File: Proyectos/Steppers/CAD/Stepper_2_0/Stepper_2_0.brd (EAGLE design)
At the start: 151.1 x 97.8 mm, 91 parts

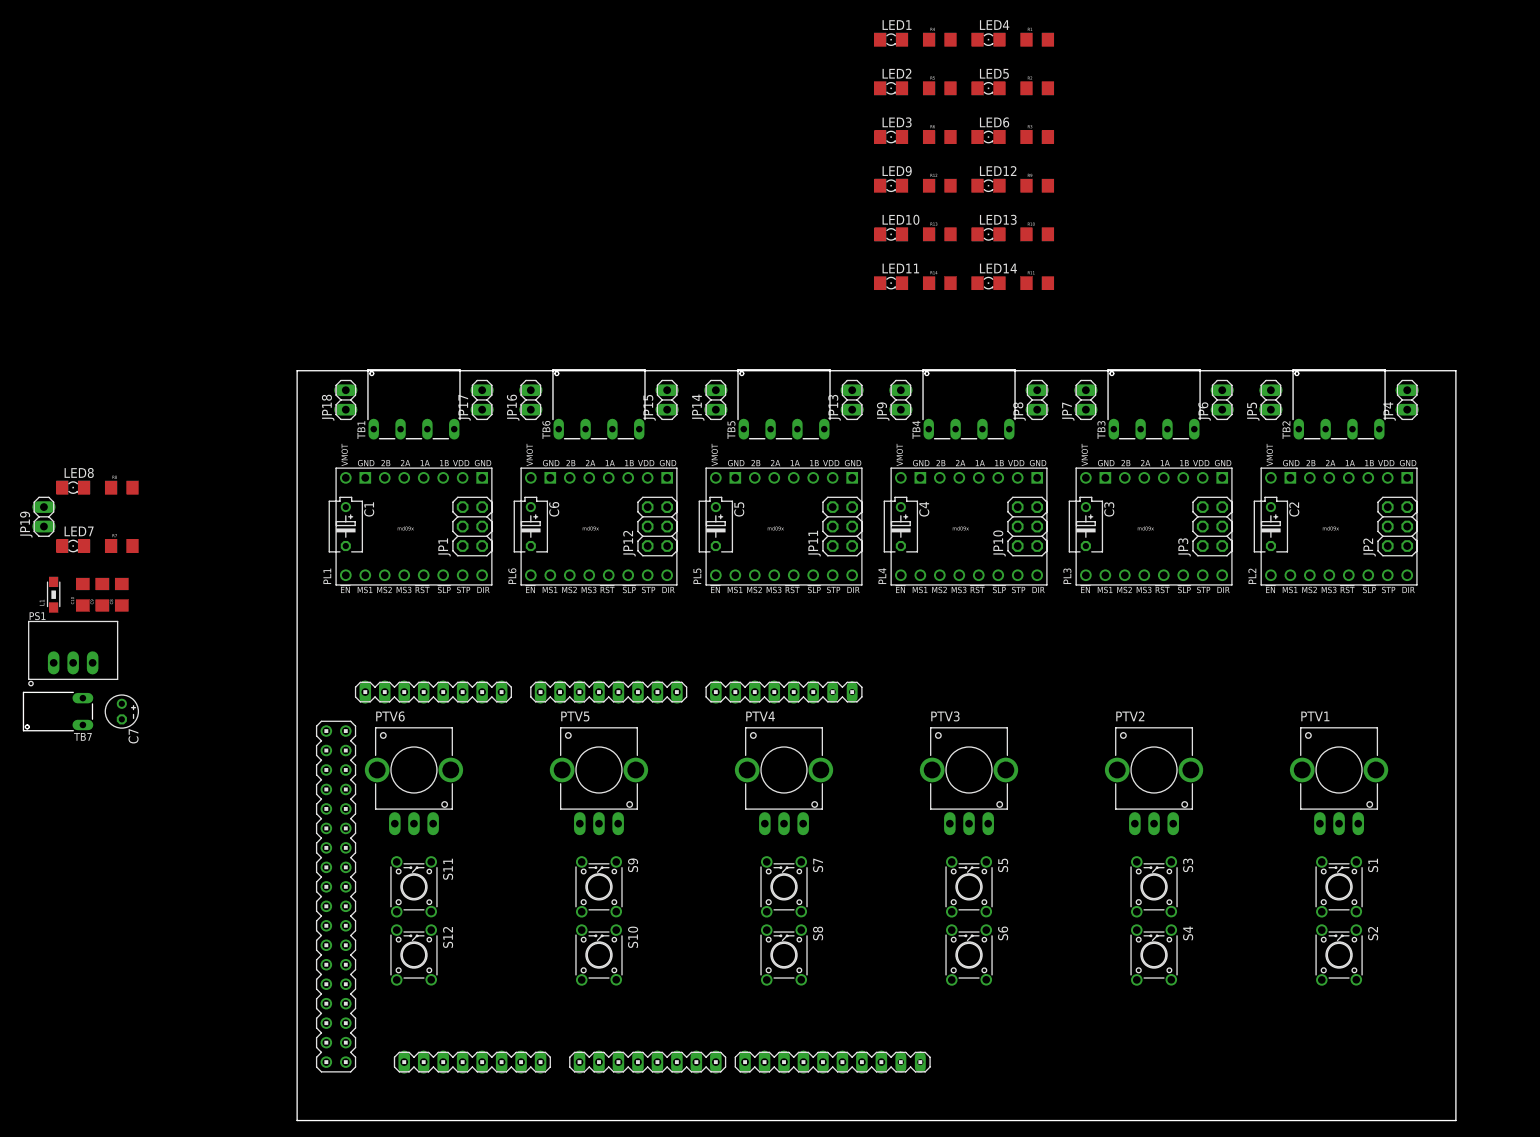
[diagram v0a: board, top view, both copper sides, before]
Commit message: Steppers:
Avance en PCB final, asignación de pines DUE.
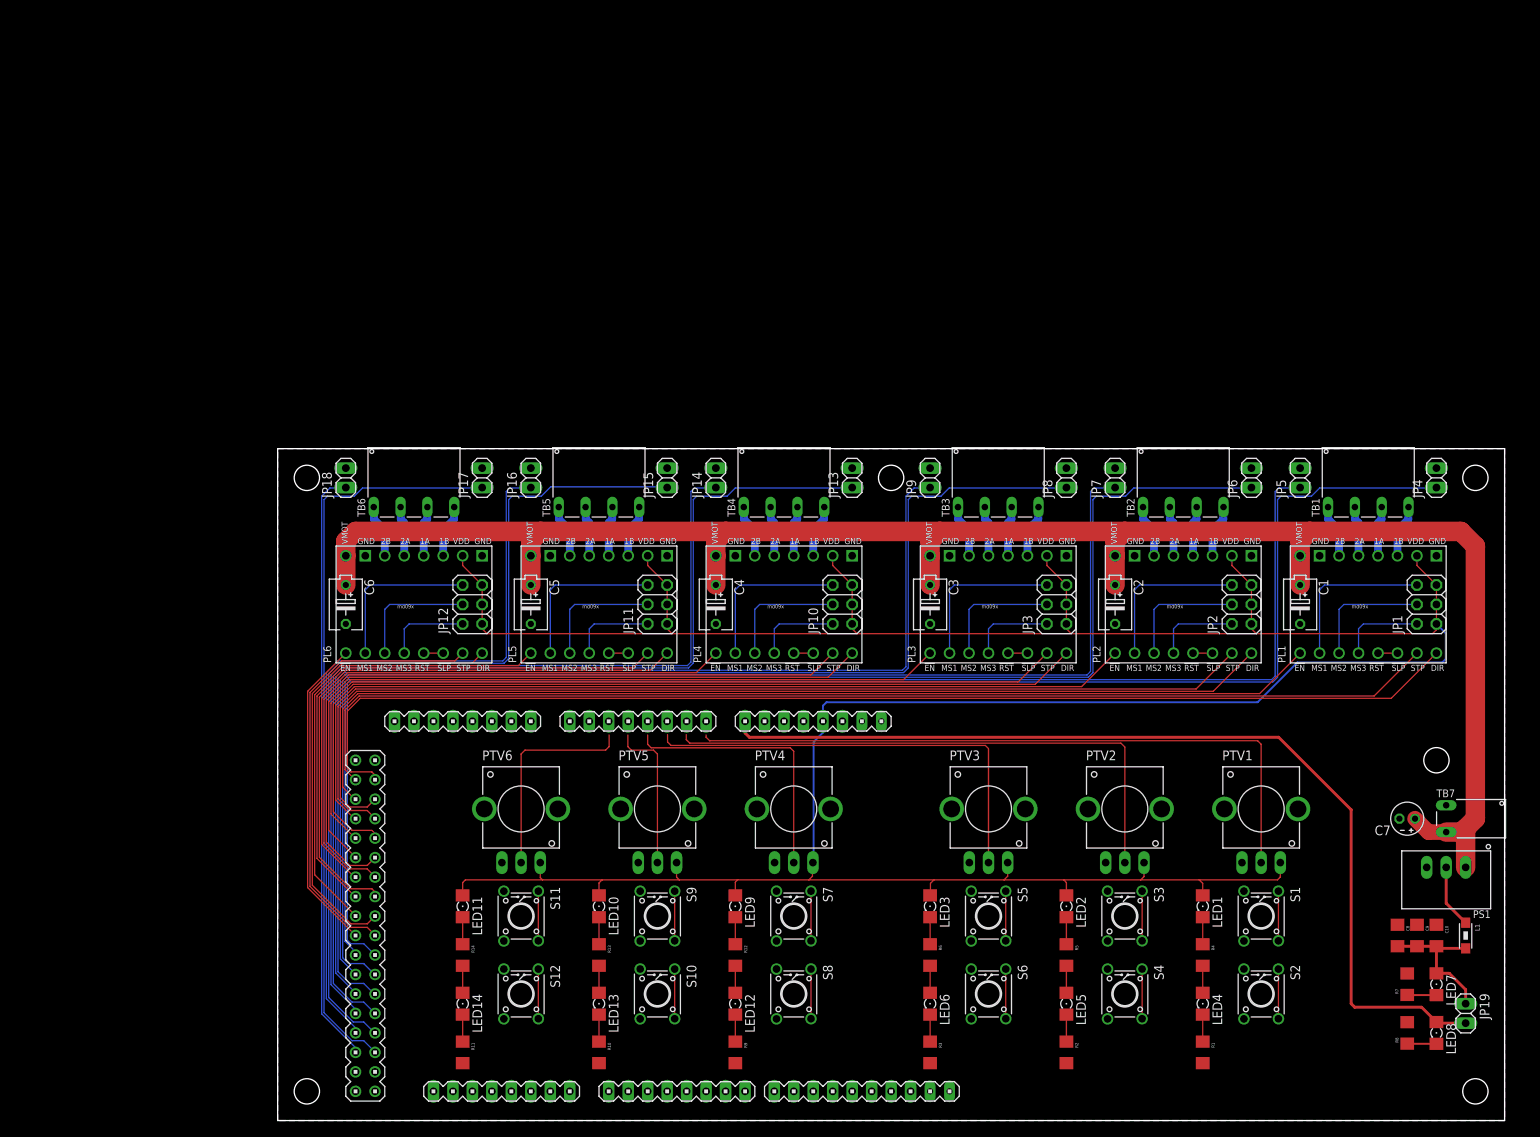
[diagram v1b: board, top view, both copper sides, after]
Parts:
- added H1, H2, H3, H4, H5, H6: STAND-OFF, SparkFun-Electromechanical:STAND-OFF
- moved JP19 196.4 mm to (152.4, 14.0), turned to 270 degrees
- moved LED8 191.5 mm to (148.6, 11.4), turned to 270 degrees
- moved L1 189.4 mm to (152.4, 24.1), turned to 270 degrees
- moved LED7 186.8 mm to (148.6, 17.8), turned to 270 degrees
- moved R8 182.1 mm to (144.8, 11.4), turned to 90 degrees
- moved C10 182.0 mm to (148.6, 24.1), turned to 270 degrees
- moved PS1 181.0 mm to (149.9, 33.0), turned to 180 degrees
- moved TB7 178.3 mm to (149.9, 39.4), turned to 270 degrees
- moved C9 177.1 mm to (146.1, 24.1), turned to 270 degrees
- moved R7 177.1 mm to (144.8, 17.8), turned to 90 degrees
- moved C8 172.2 mm to (143.5, 24.1), turned to 270 degrees
- moved C7 168.2 mm to (144.8, 39.4), turned to 180 degrees
- moved R1 133.8 mm to (118.1, 8.89), turned to 270 degrees
- moved LED4 128.8 mm to (118.1, 15.2), turned to 270 degrees
- moved R2 125.8 mm to (100.3, 8.89), turned to 270 degrees
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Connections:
- removed net N$12: LED1.A
- removed net N$14: LED2.A
- removed net N$25: LED3.A
- removed net N$36: LED9.A
- removed net N$47: LED10.A
- removed net N$63: LED11.A
- new net N$97: DUE1.23
- new net N$98: DUE1.22
- net 3V3: now also LED1.A, LED10.A, LED11.A, LED2.A, LED3.A, LED9.A
- net M1_DIR: now also DUE1.52
- net M1_EN: now also DUE1.51
- net M1_SL: now also DUE1.34
- net M1_SR: now also DUE1.35
- net M1_STEP: now also DUE1.53
- net M2_DIR: now also DUE1.50
- net M2_EN: now also DUE1.49
- net M2_SL: now also DUE1.32
- net M2_SR: now also DUE1.33
- net M2_STEP: now also DUE1.48
- net M3_DIR: now also DUE1.46
- net M3_EN: now also DUE1.45
- net M3_SL: now also DUE1.30
- net M3_SR: now also DUE1.31
- net M3_STEP: now also DUE1.47
- net M4_DIR: now also DUE1.44
- net M4_EN: now also DUE1.43
- net M4_SL: now also DUE1.28
- net M4_SR: now also DUE1.29
- net M4_STEP: now also DUE1.42
- net M5_DIR: now also DUE1.40
- net M5_EN: now also DUE1.39
- net M5_SL: now also DUE1.26
- net M5_SR: now also DUE1.27
- net M5_STEP: now also DUE1.41
- net M6_DIR: now also DUE1.38
- net M6_EN: now also DUE1.37
- net M6_SL: now also DUE1.24
- net M6_SR: now also DUE1.25
- net M6_STEP: now also DUE1.36
- net N$20: now also JP3.2; no longer JP3.6
- net N$22: now also JP3.6; no longer JP3.2
- net N$31: now also JP10.2; no longer JP10.6
- net N$33: now also JP10.6; no longer JP10.2
- net N$42: now also JP11.2; no longer JP11.6
- net N$44: now also JP11.6; no longer JP11.2
- net N$53: now also PL6.MS1; no longer PL6.MS3
- net N$55: now also PL6.MS3; no longer PL6.MS1
- net N$6: now also JP2.2; no longer JP2.6
- net N$64: now also JP1.2; no longer JP1.6
- net N$66: now also JP1.6; no longer JP1.2
- net N$8: now also JP2.6; no longer JP2.2
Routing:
- net 3V3: track 0.00 -> 435.5 mm
- net VCC: track 0.00 -> 241.9 mm
- net M1_SL: track 0.00 -> 204.1 mm
- net M1_SR: track 0.00 -> 185.3 mm
- net M2_SL: track 0.00 -> 183.4 mm
- net M2_SR: track 0.00 -> 164.4 mm
- net M3_SL: track 0.00 -> 162.4 mm
- net M1_DIR: track 0.00 -> 157.2 mm
- net M1_STEP: track 0.00 -> 152.6 mm
- net M3_SR: track 0.00 -> 143.2 mm
- net M1_EN: track 0.00 -> 140.4 mm
- net M2_DIR: track 0.00 -> 138.9 mm
- net M4_SL: track 0.00 -> 137.5 mm
- net M2_STEP: track 0.00 -> 137.4 mm
- net VIN: track 0.00 -> 126.1 mm
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- added copper zone on layer 1, net GND
- added copper zone on layer 16, net GND
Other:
- board size 151.1 x 97.8 mm -> 160 x 87.6 mm

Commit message: Steppers:
Se finaliza el esquemático y PCB de forma funcional.
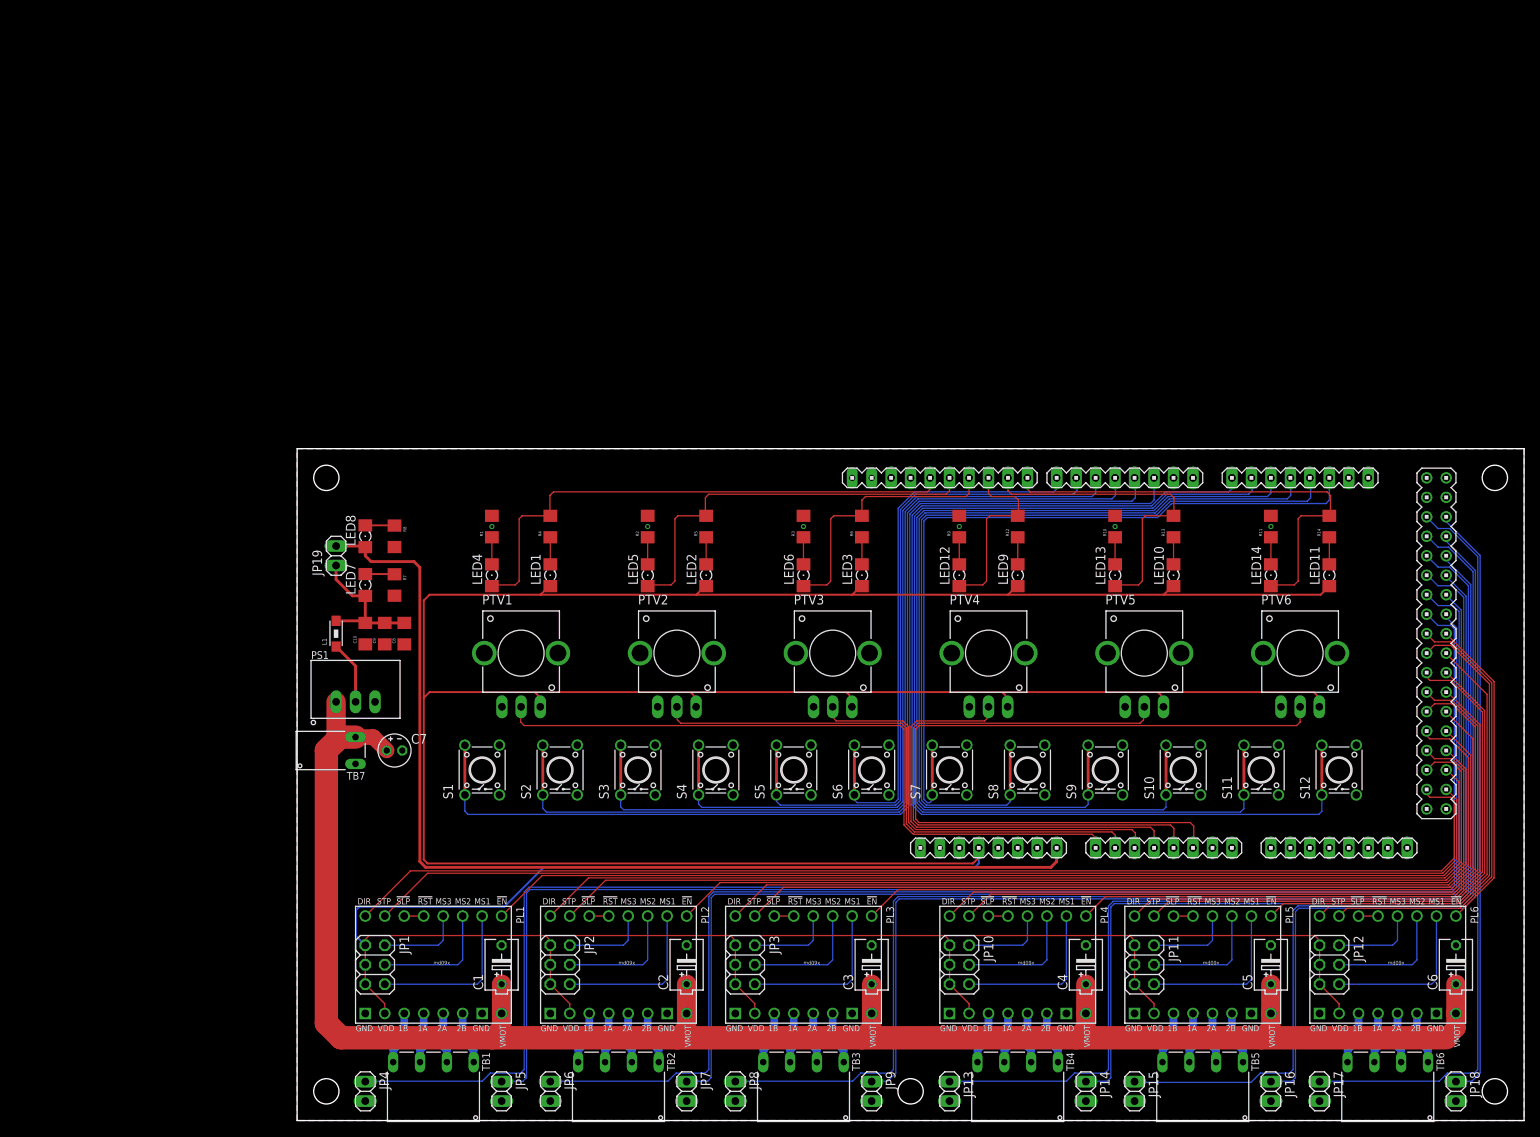
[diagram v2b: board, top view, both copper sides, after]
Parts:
- removed H6: STAND-OFF, SparkFun-Electromechanical:STAND-OFF
- moved H2 174.4 mm to (156.2, 83.8), turned to 180 degrees
- moved H3 174.4 mm to (156.2, 3.81), turned to 180 degrees
- moved H4 169.9 mm to (3.81, 3.81), turned to 180 degrees
- moved H5 169.9 mm to (3.81, 83.8), turned to 180 degrees
- moved JP18 165.4 mm to (151.1, 3.81), turned to 270 degrees
- moved JP4 161.0 mm to (8.89, 3.81), turned to 270 degrees
- moved JP19 159.0 mm to (5.08, 73.7), turned to 90 degrees
- moved LED8 154.0 mm to (8.89, 76.2), turned to 90 degrees
- moved L1 152.5 mm to (5.08, 63.5), turned to 90 degrees
- moved C6 152.2 mm to (151.1, 20.3), turned to 90 degrees
- moved LED7 149.1 mm to (8.89, 69.8), turned to 90 degrees
- moved R8 147.1 mm to (12.7, 76.2), turned to 270 degrees
- moved TB6 146.2 mm to (142.2, 7.62), turned to 180 degrees
- moved C10 145.1 mm to (8.89, 63.5), turned to 90 degrees
- moved JP1 145.0 mm to (10.2, 20.3), turned to 270 degrees
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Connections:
- removed net N$97: DUE1.23
- removed net N$98: DUE1.22
- net M1_BTNL: now also DUE1.2
- net M1_BTNR: now also DUE1.3
- net M1_LED: now also DUE1.13
- net M1_MVEL: now also DUE1.A0
- net M2_BTNL: now also DUE1.4
- net M2_BTNR: now also DUE1.5
- net M2_LED: now also DUE1.12
- net M2_MVEL: now also DUE1.A1
- net M3_BTNL: now also DUE1.6
- net M3_BTNR: now also DUE1.7
- net M3_LED: now also DUE1.11
- net M3_MVEL: now also DUE1.A2
- net M4_BTNL: now also DUE1.RX1
- net M4_BTNR: now also DUE1.TX1
- net M4_LED: now also DUE1.10
- net M4_MVEL: now also DUE1.A3
- net M5_BTNL: now also DUE1.RX2
- net M5_BTNR: now also DUE1.TX2
- net M5_LED: now also DUE1.9
- net M5_MVEL: now also DUE1.A4
- net M6_BTNL: now also DUE1.RX3
- net M6_BTNR: now also DUE1.TX3
- net M6_LED: now also DUE1.8
- net M6_MVEL: now also DUE1.A5
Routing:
- net 3V3: track 435.5 -> 648.2 mm
- net M6_BTNR: track 6.48 -> 145.1 mm
- net M1_BTNL: track 6.48 -> 140.8 mm
- net M6_BTNL: track 6.48 -> 136.5 mm
- net M5_BTNR: track 6.48 -> 127.8 mm
- net M1_BTNR: track 6.48 -> 127.6 mm
- net M5_BTNL: track 6.48 -> 119.1 mm
- net M2_BTNL: track 6.48 -> 114.2 mm
- net M4_BTNR: track 6.48 -> 110.5 mm
- net M4_BTNL: track 6.48 -> 101.8 mm
- net M2_BTNR: track 6.48 -> 100.8 mm
- net M3_BTNL: track 6.48 -> 87.6 mm
- net M6_MVEL: track 27.6 -> 103.8 mm
- net M3_BTNR: track 6.48 -> 74.3 mm
- net M1_LED: track 3.53 -> 70.2 mm
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
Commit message: Steppers:
Se añaden pads para testeo de voltajes y conexión de 5V para ventilador.
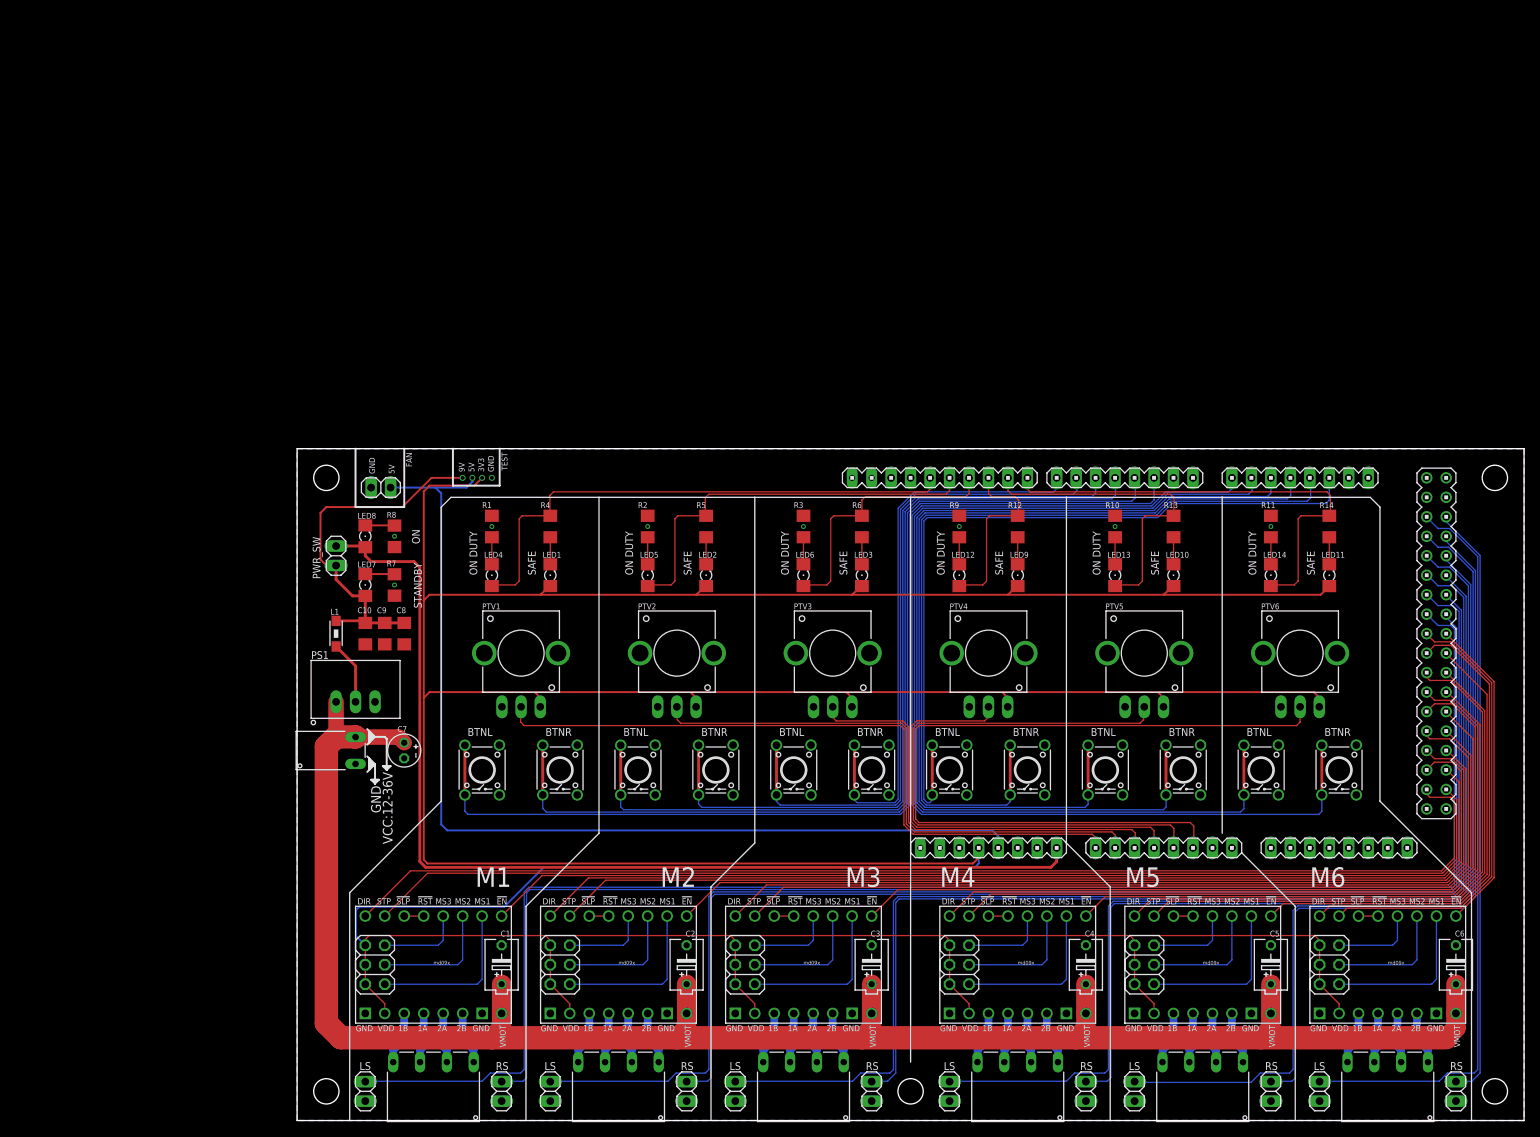
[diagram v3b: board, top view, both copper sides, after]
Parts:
- added JP20: (no value), pinhead:1X02
- moved C7 1.27 mm to (14.0, 48.3), turned to 270 degrees
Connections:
- new net 5V: DUE1.5V, JP20.2
- net GND: now also JP20.1
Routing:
- net 5V: track 0.00 -> 130.5 mm, vias 0 -> 1
- net 9V: track 19.9 -> 48.8 mm, vias 0 -> 1
- net 3V3: track 648.2 -> 670.8 mm, vias 0 -> 1
- net VCC: track 241.9 -> 243.5 mm
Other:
- board text added: "3V3"
- board text added: "5V"
- board text added: "9V"
- board text added: "BTNL"
- board text added: "BTNR"
- board text added: "FAN"
- board text added: "GND"
- board text added: "LS"
- board text added: "M1"
- board text added: "M2"
- board text added: "M3"
- board text added: "M4"
- board text added: "M5"
- board text added: "M6"
- board text added: "ON"
- board text added: "ON DUTY"
- board text added: "PWR_SW"
- board text added: "RS"
- board text added: "SAFE"
- board text added: "STANDBY"
- board text added: "TEST"
- board text added: "VCC:12-36V"
